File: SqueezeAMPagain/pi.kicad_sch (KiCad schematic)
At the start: 1 part, among them J3 Raspberry_Pi_2_3

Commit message: Update .gitignore, L_Radial_D12.0mm_P5+6+7.00mm_Fastron_11P.kicad_mod, SqueezeAMPagain.kicad_pcb, and 13 more files
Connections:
- net SCL: now also J3.5 (SCL/GPIO3)
- net SDA: now also J3.3 (SDA/GPIO2)
- net BCLK: now reaches J3.12 (GPIO18/PWM0)
- net PWM: now reaches J3.32 (PWM0/GPIO12)
- net LRCLK: now reaches J3.35 (GPIO19/MISO1)
- net DATA: now reaches J3.40 (GPIO21/SCLK1)
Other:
- note added: "No MCLK on RPi"
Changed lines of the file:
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@@
 	(generator_version "8.0")
 	(paper "A4")
-	(hierarchical_label "FS"
-		(shape input)
-		(at 57.15 82.55 0)
+	(wire
+		(pts
+			(xy 114.3 72.39) (xy 106.68 72.39)
+		)
+		(stroke
+			(width 0)
+			(type default)
+		)
+	)
+	(wire
+		(pts
+			(xy 115.57 74.93) (xy 106.68 74.93)
+		)
+		(stroke
+			(width 0)
+			(type default)
+		)
+	)
+	(text "No MCLK on RPi "
+		(exclude_from_sim no)
+		(at 27.432 76.2 0)
+		(effects
+			(font
+				(size 1.27 1.27)
+			)
+		)
+	)
+	(hierarchical_label "PWM"
+		(shape output)
+		(at 106.68 105.41 0)
 		(fields_autoplaced yes)
 		(effects
@@
 		)
 	)
-	(hierarchical_label "sdout"
-		(shape input)
-		(at 57.15 87.63 180)
+	(hierarchical_label "LRCLK"
+		(shape output)
+		(at 66.04 82.55 180)
 		(fields_autoplaced yes)
 		(effects
@@
 		)
 	)
-	(hierarchical_label "SCLK"
-		(shape input)
-		(at 57.15 77.47 0)
+	(hierarchical_label "DATA"
+		(shape output)
+		(at 66.04 87.63 180)
+		(fields_autoplaced yes)
+		(effects
+			(font
+				(size 1.27 1.27)
+			)
+			(justify right)
+		)
+	)
+	(hierarchical_label "MCLK"
+		(shape output)
+		(at 34.29 81.28 180)
+		(fields_autoplaced yes)
+		(effects
+			(font
+				(size 1.27 1.27)
+			)
+			(justify right)
+		)
+	)
+	(hierarchical_label "BCLK"
+		(shape output)
+		(at 66.04 77.47 180)
+		(fields_autoplaced yes)
+		(effects
+			(font
+				(size 1.27 1.27)
+			)
+			(justify right)
+		)
+	)
+	(hierarchical_label "SCL"
+		(shape output)
+		(at 115.57 74.93 0)
 		(fields_autoplaced yes)
 		(effects
@@
 		)
 	)
-	(hierarchical_label "SCL"
-		(shape input)
-		(at 111.76 74.93 0)
-		(fields_autoplaced yes)
-		(effects
-			(font
-				(size 1.27 1.27)
-			)
-			(justify left)
-		)
-	)
 	(hierarchical_label "SDA"
-		(shape input)
-		(at 111.76 72.39 0)
+		(shape bidirectional)
+		(at 114.3 72.39 0)
 		(fields_autoplaced yes)
 		(effects
@@
 		)
 		(instances
-			(project "squeezeampesppi"
+			(project "SqueezeAMPagain"
 				(path "/3675160b-d9e5-490e-b506-2a7966e79ed0/26fa6d25-f20f-4499-8e61-2f475408dc13"
 					(reference "#PWR07")
@@
 		)
 		(instances
-			(project "squeezeampesppi"
+			(project "SqueezeAMPagain"
 				(path "/3675160b-d9e5-490e-b506-2a7966e79ed0/26fa6d25-f20f-4499-8e61-2f475408dc13"
 					(reference "J3")
@@
 		)
 		(instances
-			(project "squeezeampesppi"
+			(project "SqueezeAMPagain"
 				(path "/3675160b-d9e5-490e-b506-2a7966e79ed0/26fa6d25-f20f-4499-8e61-2f475408dc13"
 					(reference "#PWR06")

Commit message: Update SqueezeAMPagain.kicad_pcb, SqueezeAMPagain.kicad_prl, SqueezeAMPagain.kicad_pro, and 7 more files
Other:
- note removed: "No MCLK on RPi"
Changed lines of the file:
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@@
+	(wire
+		(pts
+			(xy 60.96 77.47) (xy 66.04 77.47)
+		)
+		(stroke
+			(width 0)
+			(type default)
+		)
+	)
+	(wire
+		(pts
+			(xy 60.96 82.55) (xy 66.04 82.55)
+		)
+		(stroke
+			(width 0)
+			(type default)
+		)
+	)
+	(wire
+		(pts
+			(xy 60.96 87.63) (xy 66.04 87.63)
+		)
+		(stroke
+			(width 0)
+			(type default)
+		)
+	)
 	(wire
 		(pts
@@
 			(width 0)
 			(type default)
-		)
-	)
-	(text "No MCLK on RPi "
-		(exclude_from_sim no)
-		(at 27.432 76.2 0)
-		(effects
-			(font
-				(size 1.27 1.27)
-			)
 		)
 	)
@@
 	(hierarchical_label "LRCLK"
 		(shape output)
-		(at 66.04 82.55 180)
+		(at 60.96 82.55 180)
 		(fields_autoplaced yes)
 		(effects
@@
 	(hierarchical_label "DATA"
 		(shape output)
-		(at 66.04 87.63 180)
-		(fields_autoplaced yes)
-		(effects
-			(font
-				(size 1.27 1.27)
-			)
-			(justify right)
-		)
-	)
-	(hierarchical_label "MCLK"
-		(shape output)
-		(at 34.29 81.28 180)
+		(at 60.96 87.63 180)
 		(fields_autoplaced yes)
 		(effects
@@
 	(hierarchical_label "BCLK"
 		(shape output)
-		(at 66.04 77.47 180)
+		(at 60.96 77.47 180)
 		(fields_autoplaced yes)
 		(effects

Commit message: Update L_Radial_D12.0mm_P5+6+7.00mm_Fastron_11P.kicad_mod, SqueezeAMPagain.kicad_pcb, SqueezeAMPagain.kicad_prl, and 5 more files
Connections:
- net MOSI: now reaches J3.19 (MOSI0/GPIO10)
- net MISO: now reaches J3.21 (MISO0/GPIO9)
- net GPIO25: now reaches J3.22 (GPIO25)
- net SCLK: now reaches J3.23 (SCLK0/GPIO11)
- net ~{CE0}: now reaches J3.24 (~{CE0}/GPIO8)
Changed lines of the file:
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@@
+		)
+	)
+	(hierarchical_label "SCLK"
+		(shape output)
+		(at 106.68 100.33 0)
+		(fields_autoplaced yes)
+		(effects
+			(font
+				(size 1.27 1.27)
+			)
+			(justify left)
+		)
+	)
+	(hierarchical_label "GPIO25"
+		(shape output)
+		(at 66.04 100.33 180)
+		(fields_autoplaced yes)
+		(effects
+			(font
+				(size 1.27 1.27)
+			)
+			(justify right)
+		)
+	)
+	(hierarchical_label "~{CE0}"
+		(shape output)
+		(at 106.68 92.71 0)
+		(fields_autoplaced yes)
+		(effects
+			(font
+				(size 1.27 1.27)
+			)
+			(justify left)
+		)
+	)
+	(hierarchical_label "MOSI"
+		(shape output)
+		(at 106.68 97.79 0)
+		(fields_autoplaced yes)
+		(effects
+			(font
+				(size 1.27 1.27)
+			)
+			(justify left)
 		)
 	)
@@
 		(fields_autoplaced yes)
 		(effects
+			(font
+				(size 1.27 1.27)
+			)
+			(justify left)
+		)
+	)
+	(hierarchical_label "MISO"
+		(shape output)
+		(at 106.68 95.25 0)
+		(fields_autoplaced yes)
+		(effects

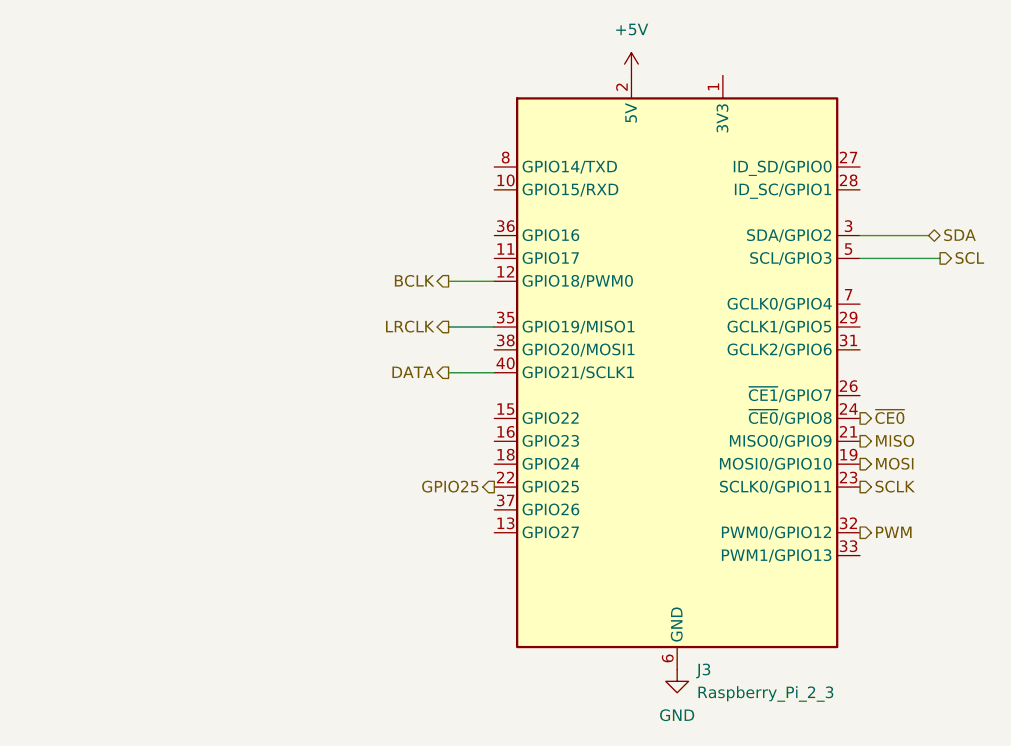
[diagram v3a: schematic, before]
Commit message: Update SqueezeAMPagain.kicad_pcb, SqueezeAMPagain.kicad_prl, SqueezeAMPagain.kicad_pro, and 5 more files
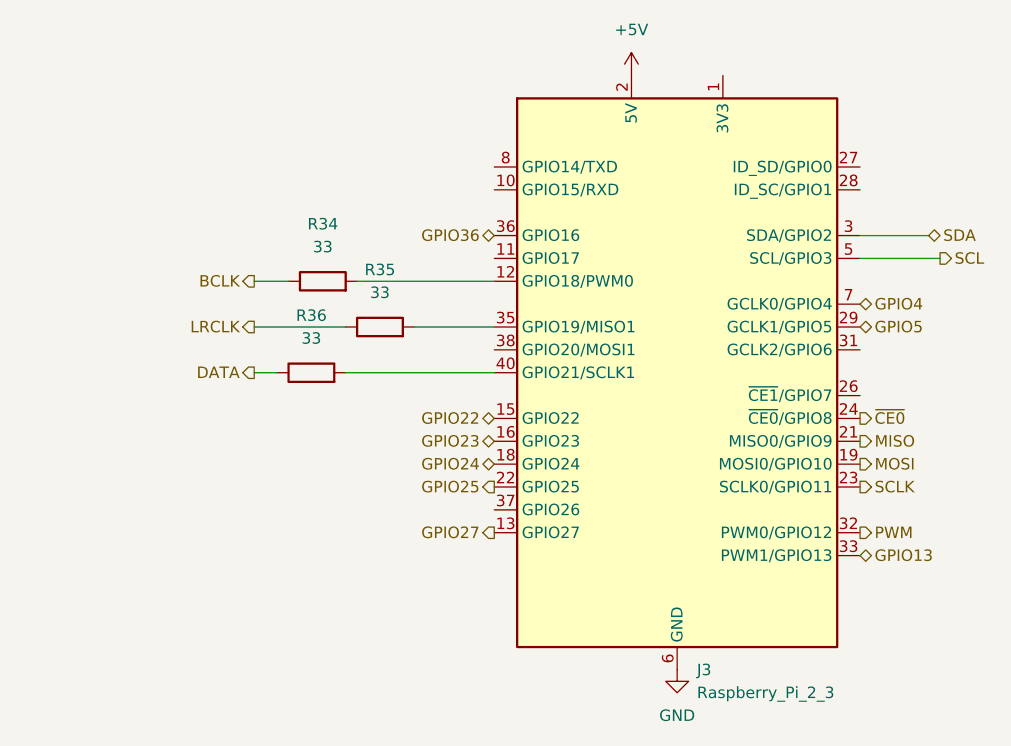
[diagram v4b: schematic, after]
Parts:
- added R34, R35, R36: 33, Resistor_SMD:R_0402_1005Metric, symbol Device:R
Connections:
- net BCLK: now also R34.1; no longer J3.12 (GPIO18/PWM0)
- net DATA: now also R36.1; no longer J3.40 (GPIO21/SCLK1)
- net LRCLK: now also R35.1; no longer J3.35 (GPIO19/MISO1)
- net GPIO27: now reaches J3.13 (GPIO27)
- net GPIO22: now reaches J3.15 (GPIO22)
- net GPIO23: now reaches J3.16 (GPIO23)
- net GPIO24: now reaches J3.18 (GPIO24)
- net GPIO5: now reaches J3.29 (GCLK1/GPIO5)
- net GPIO13: now reaches J3.33 (PWM1/GPIO13)
- net GPIO36: now reaches J3.36 (GPIO16)
- net GPIO4: now reaches J3.7 (GCLK0/GPIO4)
- new net: J3.40 (GPIO21/SCLK1), R36.2
- new net: J3.12 (GPIO18/PWM0), R34.2
- new net: J3.35 (GPIO19/MISO1), R35.2

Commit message: Update SqueezeAMPagain.kicad_pcb, SqueezeAMPagain.kicad_prl, SqueezeAMPagain.kicad_pro, and 11 more files
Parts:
- renumbered J3 to J4, R36 to R15, R34 to R16, R35 to R17
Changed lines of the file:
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@@
 		(dnp no)
 		(fields_autoplaced yes)
-		(property "Reference" "#PWR07"
+		(property "Reference" "#PWR064"
 			(at 81.28 58.42 0)
 			(effects
@@
 			(project "SqueezeAMPagain"
 				(path "/3675160b-d9e5-490e-b506-2a7966e79ed0/26fa6d25-f20f-4499-8e61-2f475408dc13"
-					(reference "#PWR07")
+					(reference "#PWR064")
 					(unit 1)
 				)
@@
 		(dnp no)
 		(fields_autoplaced yes)
-		(property "Reference" "R36"
+		(property "Reference" "R15"
 			(at 45.72 81.28 90)
 			(effects
@@
 			(project "SqueezeAMPagain"
 				(path "/3675160b-d9e5-490e-b506-2a7966e79ed0/26fa6d25-f20f-4499-8e61-2f475408dc13"
-					(reference "R36")
+					(reference "R15")
 					(unit 1)
 				)
@@
 		(dnp no)
 		(fields_autoplaced yes)
-		(property "Reference" "J3"
+		(property "Reference" "J4"
 			(at 88.5541 120.65 0)
 			(effects
@@
 			(project "SqueezeAMPagain"
 				(path "/3675160b-d9e5-490e-b506-2a7966e79ed0/26fa6d25-f20f-4499-8e61-2f475408dc13"
-					(reference "J3")
+					(reference "J4")
 					(unit 1)
 				)
@@
 		(dnp no)
 		(fields_autoplaced yes)
-		(property "Reference" "#PWR06"
+		(property "Reference" "#PWR065"
 			(at 86.36 127 0)
 			(effects
@@
 			(project "SqueezeAMPagain"
 				(path "/3675160b-d9e5-490e-b506-2a7966e79ed0/26fa6d25-f20f-4499-8e61-2f475408dc13"
-					(reference "#PWR06")
+					(reference "#PWR065")
 					(unit 1)
 				)
@@
 		(dnp no)
 		(fields_autoplaced yes)
-		(property "Reference" "R34"
+		(property "Reference" "R16"
 			(at 46.99 71.12 90)
 			(effects
@@
 			(project "SqueezeAMPagain"
 				(path "/3675160b-d9e5-490e-b506-2a7966e79ed0/26fa6d25-f20f-4499-8e61-2f475408dc13"
-					(reference "R34")
+					(reference "R16")
 					(unit 1)
 				)
@@
 		(dnp no)
 		(fields_autoplaced yes)
-		(property "Reference" "R35"
+		(property "Reference" "R17"
 			(at 53.34 76.2 90)
 			(effects
@@
 			(project "SqueezeAMPagain"
 				(path "/3675160b-d9e5-490e-b506-2a7966e79ed0/26fa6d25-f20f-4499-8e61-2f475408dc13"
-					(reference "R35")
-					(unit 1)
-				)
+					(reference "R17")
+					(unit 1)
+				)

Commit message: Update SqueezeAMPagain.kicad_pcb, SqueezeAMPagain.kicad_prl, SqueezeAMPagain.kicad_pro, and 7 more files
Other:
- note added: ""R" for Raspberry"
- moved on the sheet: R15, R16, R17
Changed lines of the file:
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@@
 	(generator_version "8.0")
 	(paper "A4")
+	(polyline
+		(pts
+			(xy 19.05 91.44) (xy 19.05 92.71)
+		)
+		(stroke
+			(width 0)
+			(type default)
+		)
+	)
+	(polyline
+		(pts
+			(xy 41.91 91.44) (xy 41.91 92.71)
+		)
+		(stroke
+			(width 0)
+			(type default)
+		)
+	)
 	(wire
 		(pts
-			(xy 50.8 77.47) (xy 66.04 77.47)
+			(xy 33.02 77.47) (xy 66.04 77.47)
 		)
 		(stroke
@@
 		)
 	)
+	(polyline
+		(pts
+			(xy 39.37 92.71) (xy 41.91 92.71)
+		)
+		(stroke
+			(width 0)
+			(type default)
+		)
+	)
 	(wire
 		(pts
-			(xy 39.37 77.47) (xy 43.18 77.47)
+			(xy 21.59 77.47) (xy 25.4 77.47)
 		)
 		(stroke
@@
 	(wire
 		(pts
-			(xy 39.37 82.55) (xy 49.53 82.55)
+			(xy 21.59 82.55) (xy 31.75 82.55)
+		)
+		(stroke
+			(width 0)
+			(type default)
+		)
+	)
+	(polyline
+		(pts
+			(xy 19.05 92.71) (xy 21.59 92.71)
 		)
 		(stroke
@@
 	(wire
 		(pts
-			(xy 57.15 82.55) (xy 66.04 82.55)
+			(xy 39.37 82.55) (xy 66.04 82.55)
 		)
 		(stroke
@@
 	(wire
 		(pts
-			(xy 39.37 87.63) (xy 41.91 87.63)
+			(xy 21.59 87.63) (xy 24.13 87.63)
 		)
 		(stroke
@@
 	(wire
 		(pts
-			(xy 49.53 87.63) (xy 66.04 87.63)
-		)
-		(stroke
-			(width 0)
-			(type default)
+			(xy 31.75 87.63) (xy 66.04 87.63)
+		)
+		(stroke
+			(width 0)
+			(type default)
+		)
+	)
+	(text "\"R\" for Raspberry"
+		(exclude_from_sim no)
+		(at 30.734 92.964 0)
+		(effects
+			(font
+				(size 1.27 1.27)
+			)
 		)
 	)
@@
 	(hierarchical_label "LRCLK"
 		(shape output)
-		(at 39.37 82.55 180)
+		(at 21.59 82.55 180)
 		(fields_autoplaced yes)
 		(effects
@@
 	(hierarchical_label "DATA"
 		(shape output)
-		(at 39.37 87.63 180)
+		(at 21.59 87.63 180)
 		(fields_autoplaced yes)
 		(effects
@@
 	(hierarchical_label "BCLK"
 		(shape output)
-		(at 39.37 77.47 180)
+		(at 21.59 77.47 180)
 		(fields_autoplaced yes)
 		(effects
@@
 	(symbol
 		(lib_id "Device:R")
-		(at 45.72 87.63 90)
+		(at 27.94 87.63 90)
 		(unit 1)
 		(exclude_from_sim no)
@@
 		(fields_autoplaced yes)
 		(property "Reference" "R15"
-			(at 45.72 81.28 90)
+			(at 27.94 81.28 90)
 			(effects
 				(font
@@
 		)
 		(property "Value" "33"
-			(at 45.72 83.82 90)
+			(at 27.94 83.82 90)
 			(effects
 				(font
@@
 		)
 		(property "Footprint" "Resistor_SMD:R_0402_1005Metric"
-			(at 45.72 89.408 90)
+			(at 27.94 89.408 90)
 			(effects
 				(font
@@
 		)
 		(property "Datasheet" "~"
-			(at 45.72 87.63 0)
+			(at 27.94 87.63 0)
 			(effects
 				(font
@@
 		)
 		(property "Description" "Resistor"
-			(at 45.72 87.63 0)
+			(at 27.94 87.63 0)
 			(effects
 				(font
@@
 	(symbol
 		(lib_id "Device:R")
-		(at 46.99 77.47 90)
+		(at 29.21 77.47 90)
 		(unit 1)
 		(exclude_from_sim no)
@@
 		(fields_autoplaced yes)
 		(property "Reference" "R16"
-			(at 46.99 71.12 90)
+			(at 29.21 71.12 90)
 			(effects
 				(font
@@
 		)
 		(property "Value" "33"
-			(at 46.99 73.66 90)
+			(at 29.21 73.66 90)
 			(effects
 				(font
@@
 		)
 		(property "Footprint" "Resistor_SMD:R_0402_1005Metric"
-			(at 46.99 79.248 90)
+			(at 29.21 79.248 90)
 			(effects
 				(font
@@
 		)
 		(property "Datasheet" "~"
-			(at 46.99 77.47 0)
+			(at 29.21 77.47 0)
 			(effects
 				(font
@@
 		)
 		(property "Description" "Resistor"
-			(at 46.99 77.47 0)
+			(at 29.21 77.47 0)
 			(effects
 				(font
@@
 	(symbol
 		(lib_id "Device:R")
-		(at 53.34 82.55 90)
+		(at 35.56 82.55 90)
 		(unit 1)
 		(exclude_from_sim no)
@@
 		(fields_autoplaced yes)
 		(property "Reference" "R17"
-			(at 53.34 76.2 90)
+			(at 35.56 76.2 90)
 			(effects
 				(font
@@
 		)
 		(property "Value" "33"
-			(at 53.34 78.74 90)
+			(at 35.56 78.74 90)
 			(effects
 				(font
@@
 		)
 		(property "Footprint" "Resistor_SMD:R_0402_1005Metric"
-			(at 53.34 84.328 90)
+			(at 35.56 84.328 90)
 			(effects
 				(font
@@
 		)
 		(property "Datasheet" "~"
-			(at 53.34 82.55 0)
+			(at 35.56 82.55 0)
 			(effects
 				(font
@@
 		)
 		(property "Description" "Resistor"
-			(at 53.34 82.55 0)
-			(effects
-				(font
+			(at 35.56 82.55 0)
+			(effects
+				(font

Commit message: Update SqueezeAMPagain.kicad_pcb, SqueezeAMPagain.kicad_prl, SqueezeAMPagain.kicad_pro, and 11 more files
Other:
- title: (none) -> SqueezeAMP_{again}
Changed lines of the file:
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@@
 	(generator_version "8.0")
 	(paper "A4")
+	(title_block
+		(title "SqueezeAMP_{again}")
+		(date "2024-08-23")
+		(rev "1.0")
+	)
 	(polyline
 		(pts
